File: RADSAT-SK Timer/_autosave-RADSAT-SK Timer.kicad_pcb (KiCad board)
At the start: 2 copper layers, 90.2 x 95.9 mm, 102 parts, among them J101 Conn_02x26_Odd_Even, J103 Conn_02x26_Odd_Even, J201 Conn_01x04, J202 USB_B_Micro, J203 Conn_01x02, J204 Conn_01x02, J205 Conn_01x02, J206 Conn_01x02, J207 Conn_01x02, Q101 IRLML2060, Q102 IRLML2060, Q103 IRLML2060, Q104 IRLML2060, Q105 IRLML2060, Q106 IRLML2060, Q107 IRLML2060, Q108 IRLML2060, Q109 IRLML2060, Q201 IRLML2060, Q202 IRLML2060, SW201 SW_Push, SW202 SW_Push, SW203 SW_Push, SW204 SW_Push, SW205 SW_Push, SW206 SW_Push, U101 LM397MF, U102 LM397MF, U103 LM397MF, U104 CD4052B, U202 LTC3440EMSPBF

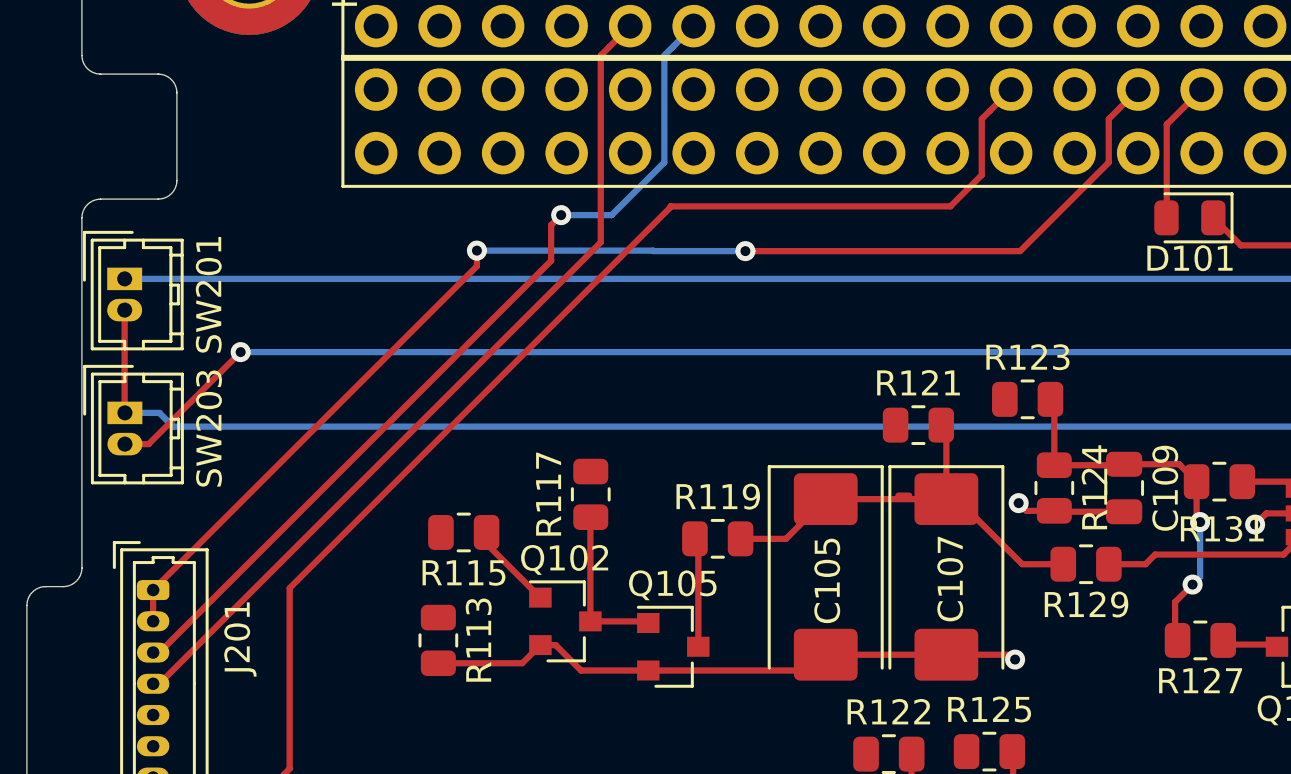
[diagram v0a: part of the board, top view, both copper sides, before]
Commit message: Change to the 7 pin Antenna on the PCB
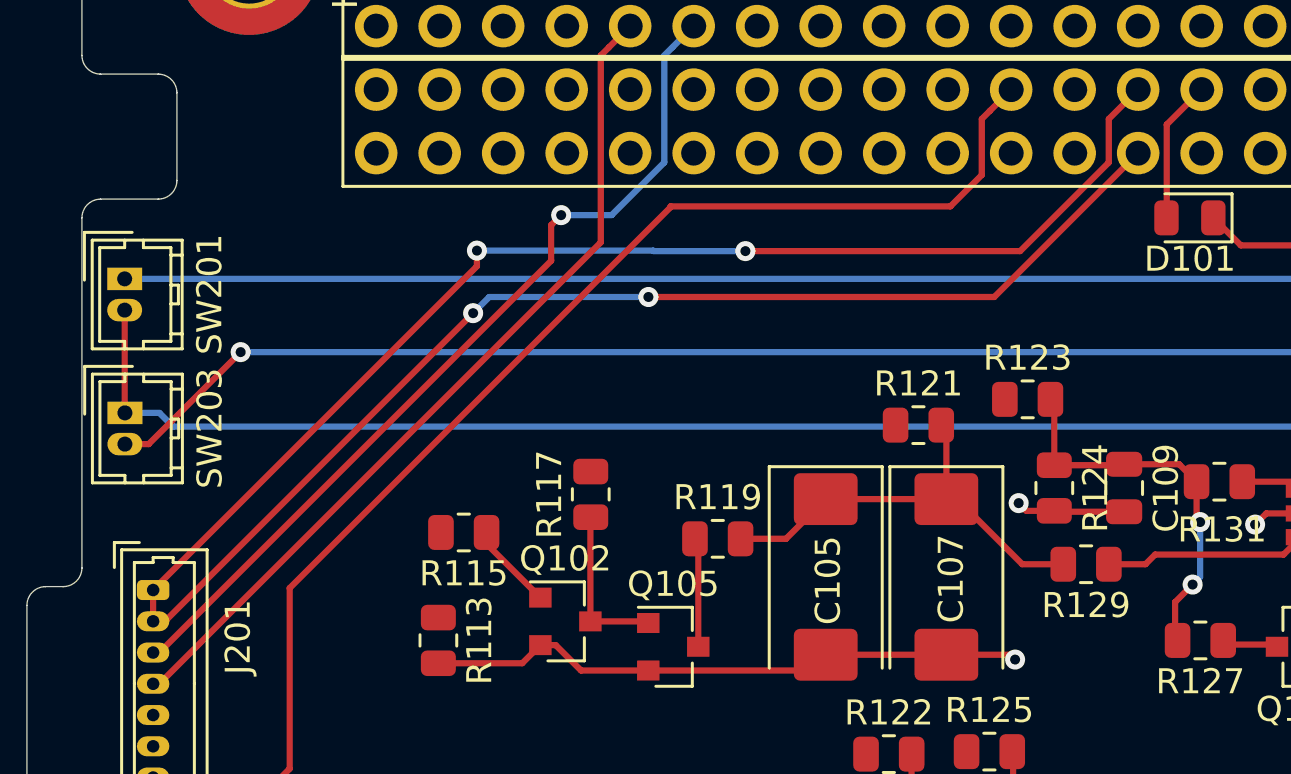
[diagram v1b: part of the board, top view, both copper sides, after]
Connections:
- J101 pad 27: (no net) -> +3V3
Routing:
- net +3V3: track 50.3 -> 97.5 mm, vias 2 -> 4
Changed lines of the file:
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@@
     (thickness 1.6)
     (drawings 55)
-    (tracks 526)
+    (tracks 533)
     (zones 0)
     (modules 102)
@@
     (mod_text_size 1 1)
     (mod_text_width 0.15)
-    (pad_size 0.8 1.3)
-    (pad_drill 0.5)
+    (pad_size 1.7 1.7)
+    (pad_drill 1)
     (pad_to_mask_clearance 0)
     (aux_axis_origin 125 50)
@@
     (pad 28 thru_hole oval (at -2.54 33.02 270) (size 1.7 1.7) (drill 1) (layers *.Cu *.Mask)
       (net 41 +3V3))
-    (pad 27 thru_hole oval (at 0 33.02 270) (size 1.7 1.7) (drill 1) (layers *.Cu *.Mask))
+    (pad 27 thru_hole oval (at 0 33.02 270) (size 1.7 1.7) (drill 1) (layers *.Cu *.Mask)
+      (net 41 +3V3))
     (pad 26 thru_hole oval (at -2.54 30.48 270) (size 1.7 1.7) (drill 1) (layers *.Cu *.Mask)
       (net 39 "Net-(D101-Pad2)"))
@@
   (segment (start 74.64414 79.104024) (end 76.28364 79.104024) (width 0.25) (layer F.Cu) (net 5))
   (segment (start 72.03964 76.499524) (end 74.64414 79.104024) (width 0.25) (layer F.Cu) (net 5))
-  (segment (start 69.68814 76.359524) (end 70.11964 76.359524) (width 0.25) (layer F.Cu) (net 5))
   (segment (start 63.047107 91.378024) (end 64.476607 89.948524) (width 0.25) (layer F.Cu) (net 6))
   (segment (start 61.47664 91.378024) (end 63.047107 91.378024) (width 0.25) (layer F.Cu) (net 6))
@@
   (segment (start 78.104999 63.034003) (end 74.559002 66.58) (width 0.25) (layer F.Cu) (net 41))
   (segment (start 79.28 60.12) (end 78.104999 61.295001) (width 0.25) (layer F.Cu) (net 41))
-  (segment (start 78.104999 61.295001) (end 78.104999 63.034003) (width 0.25) (layer F.Cu) (net 41))
   (segment (start 59.9 66.58) (end 63.57 66.58) (width 0.25) (layer B.Cu) (net 41))
   (segment (start 52.83 66.56) (end 59.88 66.56) (width 0.25) (layer B.Cu) (net 41))
@@
   (segment (start 52.83 67.185) (end 39.878 80.137) (width 0.25) (layer F.Cu) (net 41))
   (segment (start 52.83 66.56) (end 52.83 67.185) (width 0.25) (layer F.Cu) (net 41))
+  (segment (start 78.104999 61.295001) (end 78.104999 63.034003) (width 0.25) (layer F.Cu) (net 41))
+  (via (at 59.69 68.415) (size 0.8) (drill 0.4) (layers F.Cu B.Cu) (net 41))
+  (segment (start 79.28 62.66) (end 73.525 68.415) (width 0.25) (layer F.Cu) (net 41))
+  (segment (start 73.525 68.415) (end 59.69 68.415) (width 0.25) (layer F.Cu) (net 41))
+  (via (at 52.678347 69.061347) (size 0.8) (drill 0.4) (layers F.Cu B.Cu) (net 41))
+  (segment (start 59.69 68.415) (end 53.324694 68.415) (width 0.25) (layer B.Cu) (net 41))
+  (segment (start 53.324694 68.415) (end 52.678347 69.061347) (width 0.25) (layer B.Cu) (net 41))
   (segment (start 39.878 81.387) (end 39.878 80.137) (width 0.25) (layer F.Cu) (net 41))
+  (segment (start 40.352694 81.387) (end 39.878 81.387) (width 0.25) (layer F.Cu) (net 41))
+  (segment (start 52.678347 69.061347) (end 40.352694 81.387) (width 0.25) (layer F.Cu) (net 41))
   (segment (start 58.110001 58.429999) (end 58.96 57.58) (width 0.25) (layer F.Cu) (net 42))
   (segment (start 57.784999 58.755001) (end 58.110001 58.429999) (width 0.25) (layer F.Cu) (net 42))
